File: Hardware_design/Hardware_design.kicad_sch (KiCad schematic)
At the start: 46 parts, among them IC1 ESP32-S3-WROOM-1-N16, J1 FTSH-103-01-F-D, J2 SBH11-PBPC-D05-ST-BK, J3 54-00131, SW1 TL3301FF160QG, SW2 TL3301FF160QG, U1 LS7366R-S, U2 TXB0104DR, U3 LP3875EMP-3.3

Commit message: Index problem solved and some progress made
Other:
- sheet Buttons_circuits ports: added DIO_INDEX; removed none
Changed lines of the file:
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@@
 	(wire
 		(pts
+			(xy 52.07 234.95) (xy 55.88 234.95)
+		)
+		(stroke
+			(width 0)
+			(type default)
+		)
+	)
+	(wire
+		(pts
 			(xy 123.19 83.82) (xy 123.19 80.01)
 		)
@@
 		)
 	)
+	(label "INDEX"
+		(at 52.07 234.95 180)
+		(effects
+			(font
+				(size 1.27 1.27)
+			)
+			(justify right bottom)
+		)
+	)
 	(label "ESP_RXD"
 		(at 297.18 68.58 0)
@@
 	(sheet
 		(at 55.88 208.28)
-		(size 55.88 38.1)
+		(size 55.88 36.83)
 		(exclude_from_sim no)
 		(in_bom yes)
@@
 		)
 		(property "Sheetfile" "Buttons_circuits.kicad_sch"
-			(at 55.88 246.9646 0)
+			(at 55.88 245.6946 0)
 			(show_name no)
 			(do_not_autoplace no)
@@
 			)
 		)
+		(pin "DIO_INDEX" output
+			(at 55.88 234.95 180)
+			(effects
+				(font
+					(size 1.27 1.27)
+				)
+				(justify left)
+			)
+		)

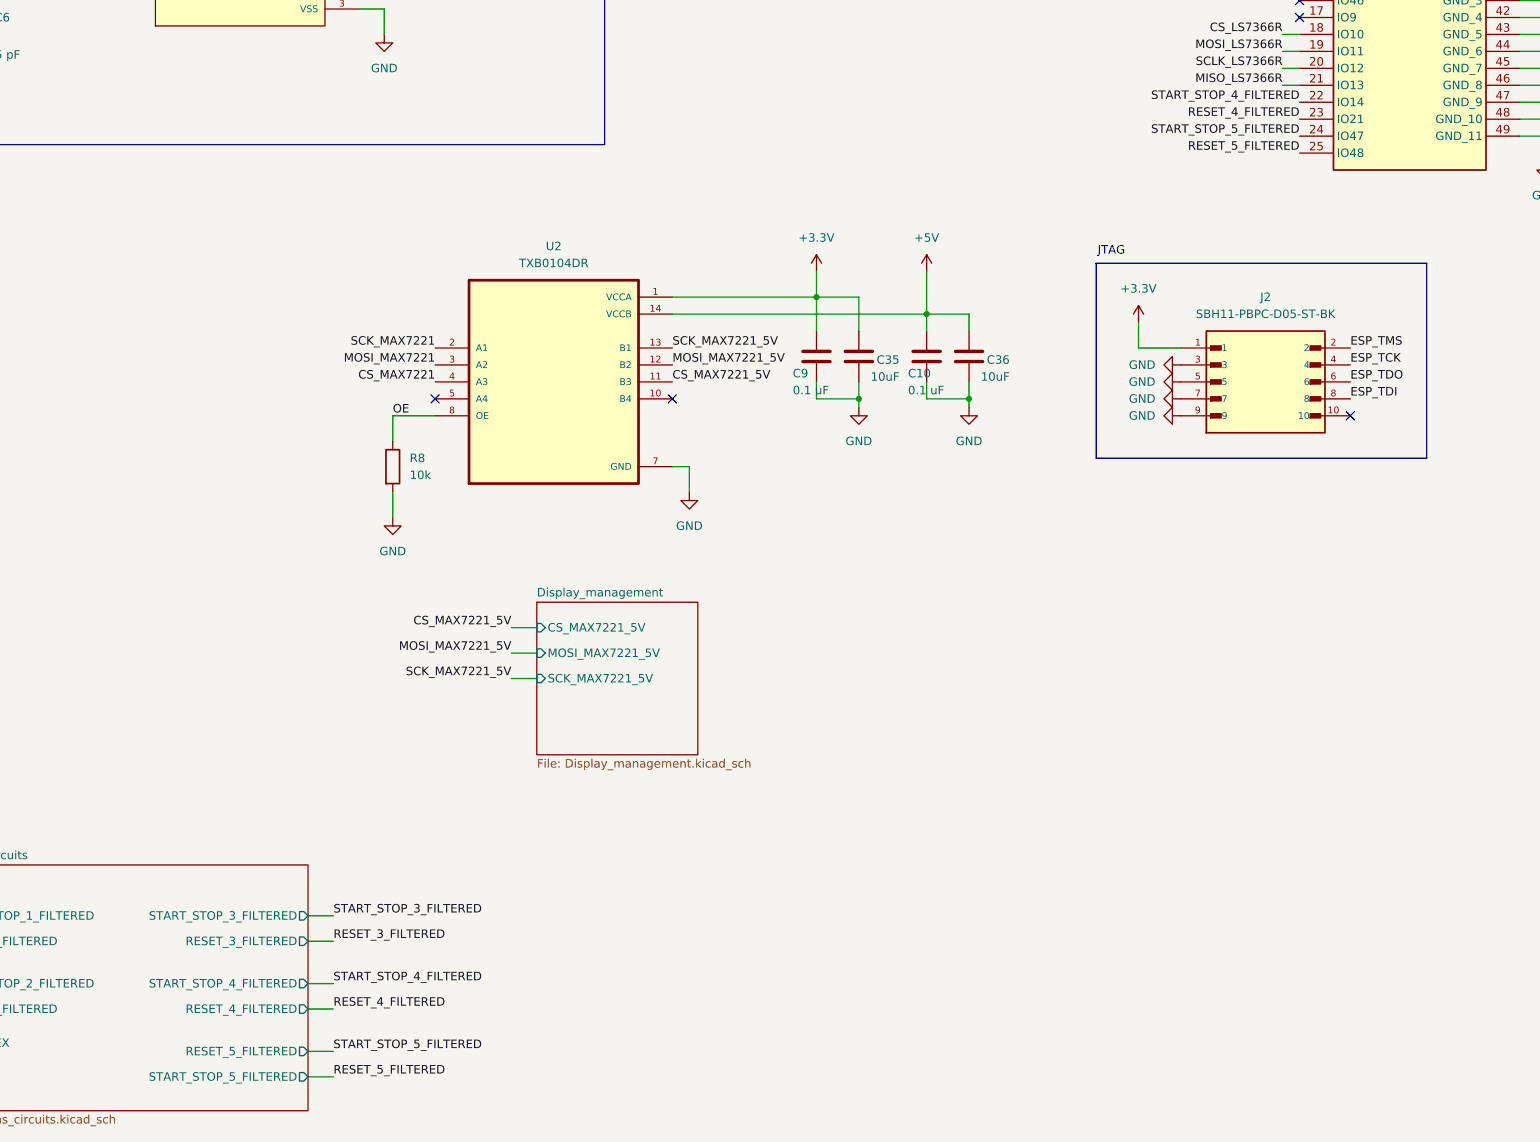
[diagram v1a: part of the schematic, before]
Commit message: big update
coper zones already set, edgecuts set, all components placed, we are just missing the routing
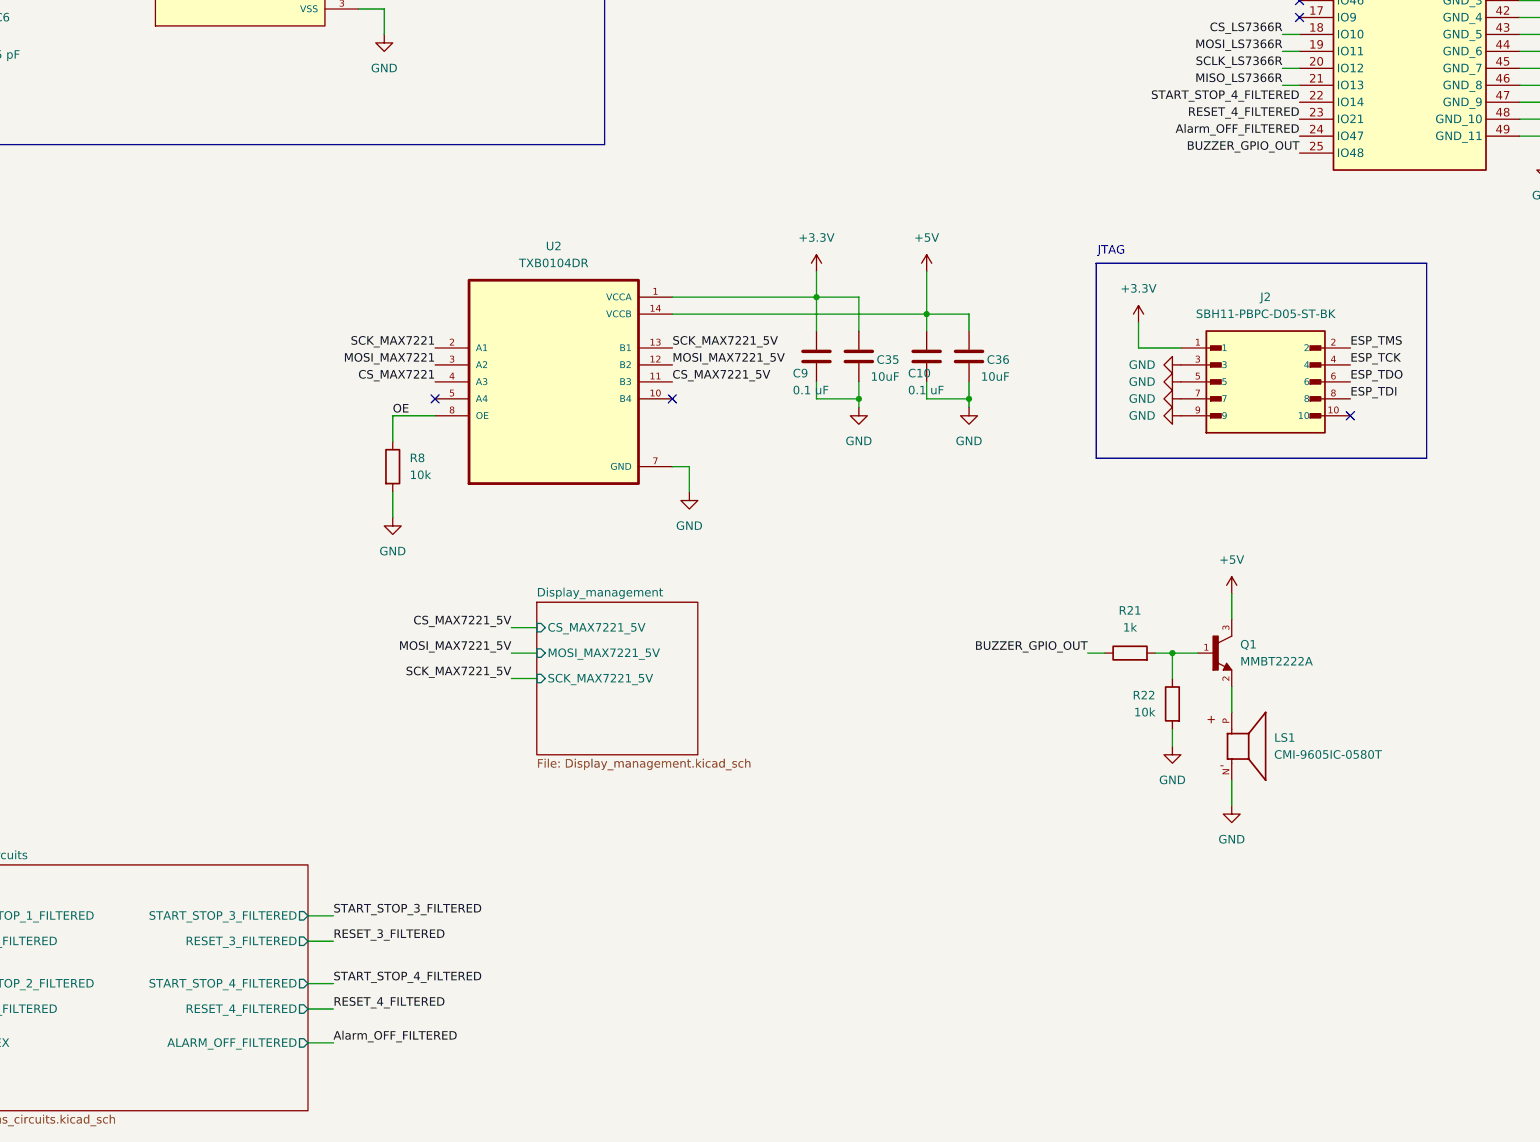
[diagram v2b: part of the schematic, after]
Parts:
- added LS1: CMI-9605IC-0580T, Footprints:BUZZER_CMI-9605IC-0580T, symbol BUZZER_CMI-9605IC-0580T:CMI-9605IC-0580T
- added Q1: MMBT2222A, Footprints:TRANSISTOR_MMBT2222A, symbol TRANSISTOR_MMBT2222A:MMBT2222A
- added R21: 1k, Footprints:0805_RES_RESC2012X60N, symbol Device:R
- added R22: 10k, Footprints:0805_RES_RESC2012X60N, symbol Device:R
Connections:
- net +5V: now also Q1.3
- net GND: now also LS1.N, R22.2
- net RESET_5_FILTERED renamed BUZZER_GPIO_OUT
- net BUZZER_GPIO_OUT: now also R21.1
- net START_STOP_5_FILTERED renamed Alarm_OFF_FILTERED
- new net: LS1.P, Q1.2
- new net: Q1.1, R21.2, R22.1
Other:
- sheet Buttons_circuits ports: added ALARM_OFF_FILTERED; removed RESET_5_FILTERED, START_STOP_5_FILTERED

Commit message: update
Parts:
- removed J2: SBH11-PBPC-D05-ST-BK, Footprints:JTAG_2.54_SBH11-PBPC-D05-ST-BK, symbol JTAG_2.54_SBH11-PBPC-D05-ST-BK:SBH11-PBPC-D05-ST-BK
- added J2: Conn_01x04_Pin, Footprints:Jtag_pins, symbol Connector:Conn_01x04_Pin
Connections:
- net ESP_TCK: now also J2.2 (Pin_2)
- net ESP_TDI: now also J2.4 (Pin_4)
- net ESP_TDO: now also J2.3 (Pin_3)
- net ESP_TMS: now also J2.1 (Pin_1)
- no-connect marks 18 -> 17

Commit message: almost finished
just missing final conections and verification of constrains for fabrication
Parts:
- J2: footprint Footprints:Jtag_pins -> Footprints:4_pin_FTR-104-01-L-S
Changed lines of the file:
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@@
 			)
 		)
-		(property "Footprint" "Footprints:Jtag_pins"
+		(property "Footprint" "Footprints:4_pin_FTR-104-01-L-S"
 			(at 252.73 130.81 0)
 			(hide yes)
